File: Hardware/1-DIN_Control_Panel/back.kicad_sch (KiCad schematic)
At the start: 44 parts, among them J1 Mode LEDs, J1 Selector Knob Connector, J2 Rotary Switch 1x7, J3 2x05 Molex Micro-Fit 3.0 43045, J4 UART Expansion, J5 SW - Aux Jump-Start, J6 SW - Battery Bypass, J7 SW - Master Power, J8 Pot/SW - Brightness, K1 FINDER-40.52, U12 LM324DR, U13 12V->5V Variable Boost Buck C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, U5 LTV-847S, U6 LTV-847S

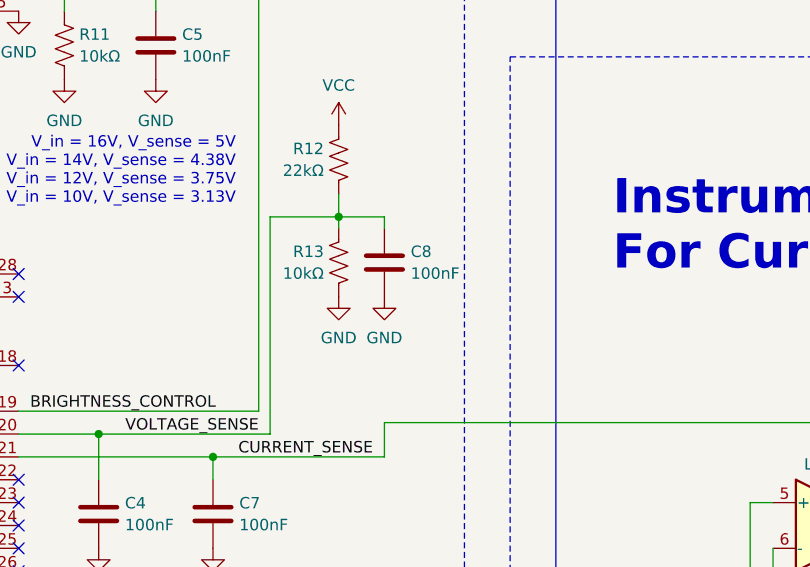
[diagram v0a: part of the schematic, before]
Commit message: Finished routing of rear board
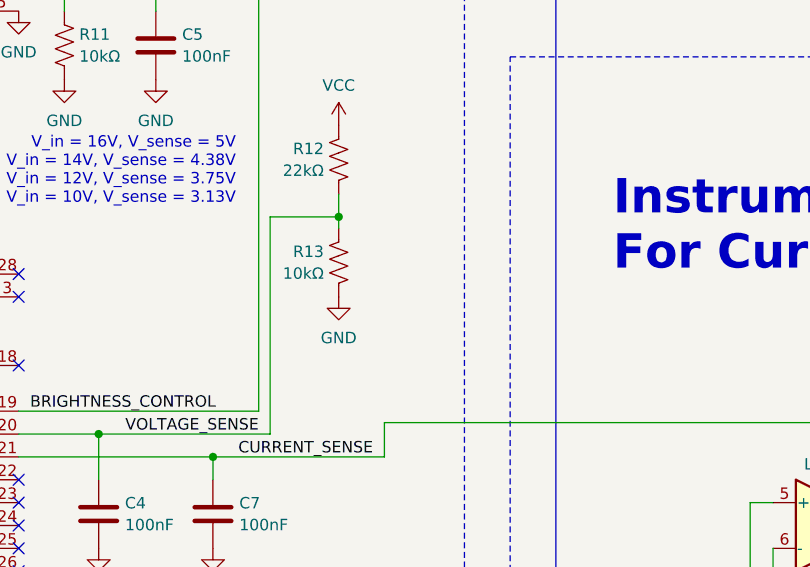
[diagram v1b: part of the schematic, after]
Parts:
- removed C8: 100nF, Capacitor_SMD:C_0603_1608Metric_Pad1.08x0.95mm_HandSolder, symbol Device:C
- C11, C14: footprint Capacitor_SMD:C_0603_1608Metric_Pad1.08x0.95mm_HandSolder -> Capacitor_SMD:C_1206_3216Metric_Pad1.33x1.80mm_HandSolder
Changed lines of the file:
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@@
     (stroke (width 0) (type default))
   )
-  (wire (pts (xy 256.54 116.84) (xy 251.46 116.84))
-    (stroke (width 0) (type default))
-  )
   (wire (pts (xy 360.68 40.64) (xy 360.68 39.37))
     (stroke (width 0) (type default))
   )
-  (wire (pts (xy 256.54 118.11) (xy 256.54 116.84))
-    (stroke (width 0) (type default))
-  )
   (wire (pts (xy 281.94 170.18) (xy 297.18 170.18))
     (stroke (width 0) (type default))
@@
       (effects (font (size 1.27 1.27)) (justify right))
     )
-    (property "Footprint" "Capacitor_SMD:C_0603_1608Metric_Pad1.08x0.95mm_HandSolder" (at 368.6048 46.99 0)
+    (property "Footprint" "Capacitor_SMD:C_1206_3216Metric_Pad1.33x1.80mm_HandSolder" (at 368.6048 46.99 0)
       (effects (font (size 1.27 1.27)) hide)
     )
@@
     )
   )
-  (symbol (lib_id "power:GND") (at 256.54 125.73 0) (unit 1)
-    (in_bom yes) (on_board yes) (dnp no) (fields_autoplaced)
-    (property "Reference" "#PWR021" (at 256.54 132.08 0)
-      (effects (font (size 1.27 1.27)) hide)
-    )
-    (property "Value" "GND" (at 256.54 130.2925 0)
-      (effects (font (size 1.27 1.27)))
-    )
-    (property "Footprint" "" (at 256.54 125.73 0)
-      (effects (font (size 1.27 1.27)) hide)
-    )
-    (property "Datasheet" "" (at 256.54 125.73 0)
-      (effects (font (size 1.27 1.27)) hide)
-    )
-    (pin "1")
-    (instances
-      (project "1-DIN_Control_Panel"
-        (path "/9d6c5460-8470-44bf-9076-df961456f999"
-          (reference "#PWR021") (unit 1)
-        )
-        (path "/9d6c5460-8470-44bf-9076-df961456f999/79705e83-d37e-491a-a216-1b060693c97a"
-          (reference "#PWR021") (unit 1)
-        )
-      )
-    )
-  )
   (symbol (lib_id "power:GND") (at 220.98 101.6 0) (mirror y) (unit 1)
     (in_bom yes) (on_board yes) (dnp no) (fields_autoplaced)
@@
     )
   )
-  (symbol (lib_id "Device:C") (at 256.54 121.92 0) (unit 1)
-    (in_bom yes) (on_board yes) (dnp no) (fields_autoplaced)
-    (property "Reference" "C8" (at 259.461 120.7079 0)
-      (effects (font (size 1.27 1.27)) (justify left))
-    )
-    (property "Value" "100nF" (at 259.461 123.1321 0)
-      (effects (font (size 1.27 1.27)) (justify left))
-    )
-    (property "Footprint" "Capacitor_SMD:C_0603_1608Metric_Pad1.08x0.95mm_HandSolder" (at 257.5052 125.73 0)
-      (effects (font (size 1.27 1.27)) hide)
-    )
-    (property "Datasheet" "~" (at 256.54 121.92 0)
-      (effects (font (size 1.27 1.27)) hide)
-    )
-    (pin "1")
-    (pin "2")
-    (instances
-      (project "1-DIN_Control_Panel"
-        (path "/9d6c5460-8470-44bf-9076-df961456f999"
-          (reference "C8") (unit 1)
-        )
-        (path "/9d6c5460-8470-44bf-9076-df961456f999/79705e83-d37e-491a-a216-1b060693c97a"
-          (reference "C8") (unit 1)
-        )
-      )
-    )
-  )
   (symbol (lib_id "power:GND") (at 251.46 125.73 0) (unit 1)
     (in_bom yes) (on_board yes) (dnp no) (fields_autoplaced)
@@
       (effects (font (size 1.27 1.27)) (justify right))
     )
-    (property "Footprint" "Capacitor_SMD:C_0603_1608Metric_Pad1.08x0.95mm_HandSolder" (at 328.6252 45.72 0)
+    (property "Footprint" "Capacitor_SMD:C_1206_3216Metric_Pad1.33x1.80mm_HandSolder" (at 328.6252 45.72 0)
       (effects (font (size 1.27 1.27)) hide)
     )

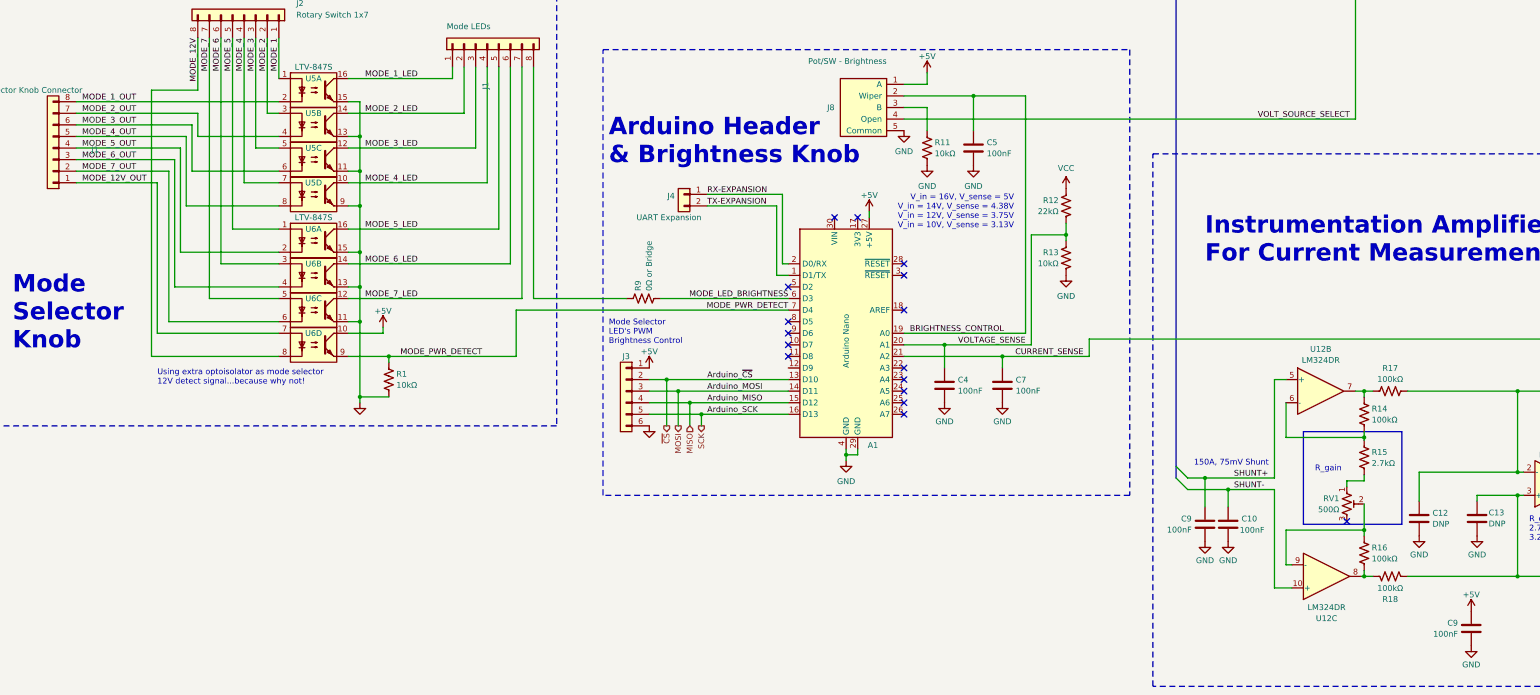
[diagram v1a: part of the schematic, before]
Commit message: Finished routing front panel
Realized that I don't know how optocouplers work, so I need to replace them with transistors or something now
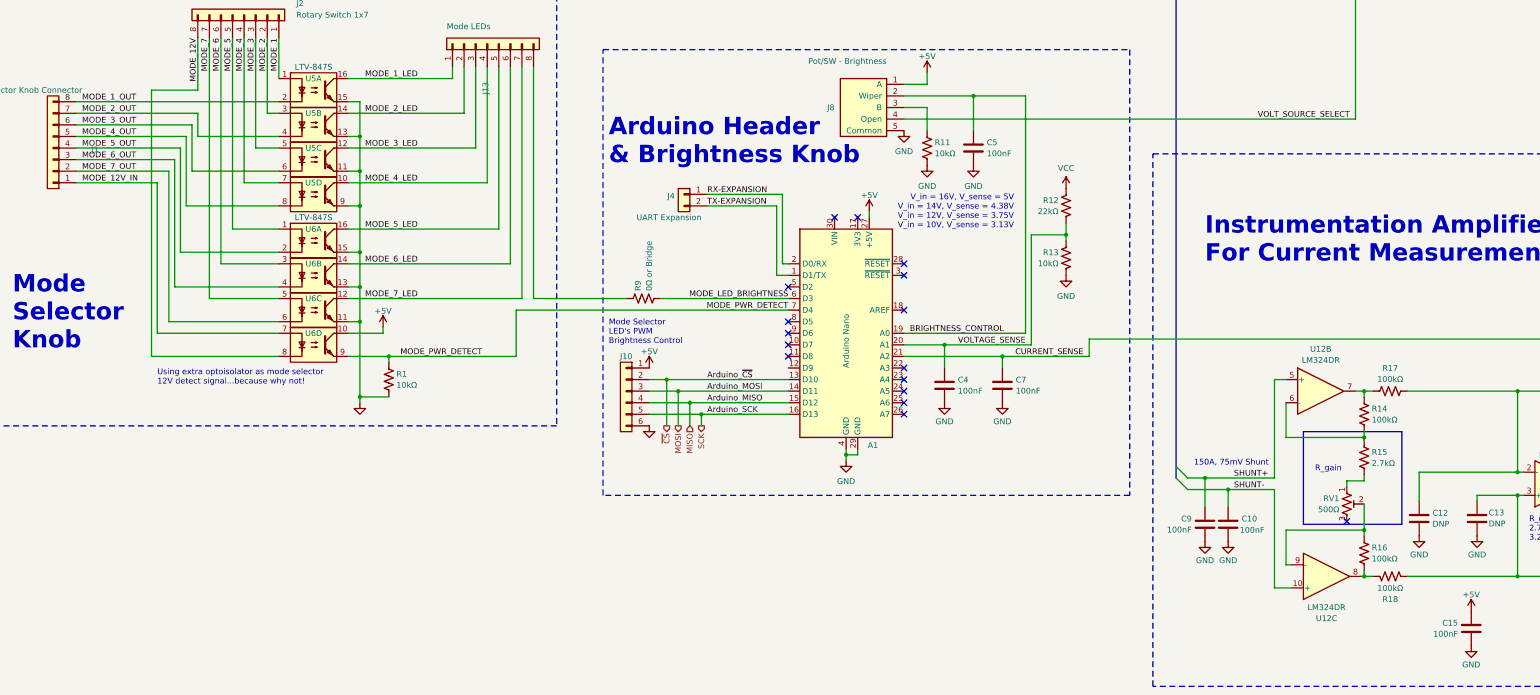
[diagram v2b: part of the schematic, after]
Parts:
- C11, C14: footprint Capacitor_SMD:C_1206_3216Metric_Pad1.33x1.80mm_HandSolder -> Capacitor_Tantalum_SMD:CP_EIA-3528-21_Kemet-B_Pad1.50x2.35mm_HandSolder
- F1: footprint Fuse:Fuse_Bourns_MF-RG300 -> Fuse:Fuse_1812_4532Metric_Pad1.30x3.40mm_HandSolder
- renumbered C9 to C15, J3 to J10, J1 to J13
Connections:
- net MODE_12V_OUT renamed MODE_12V_IN

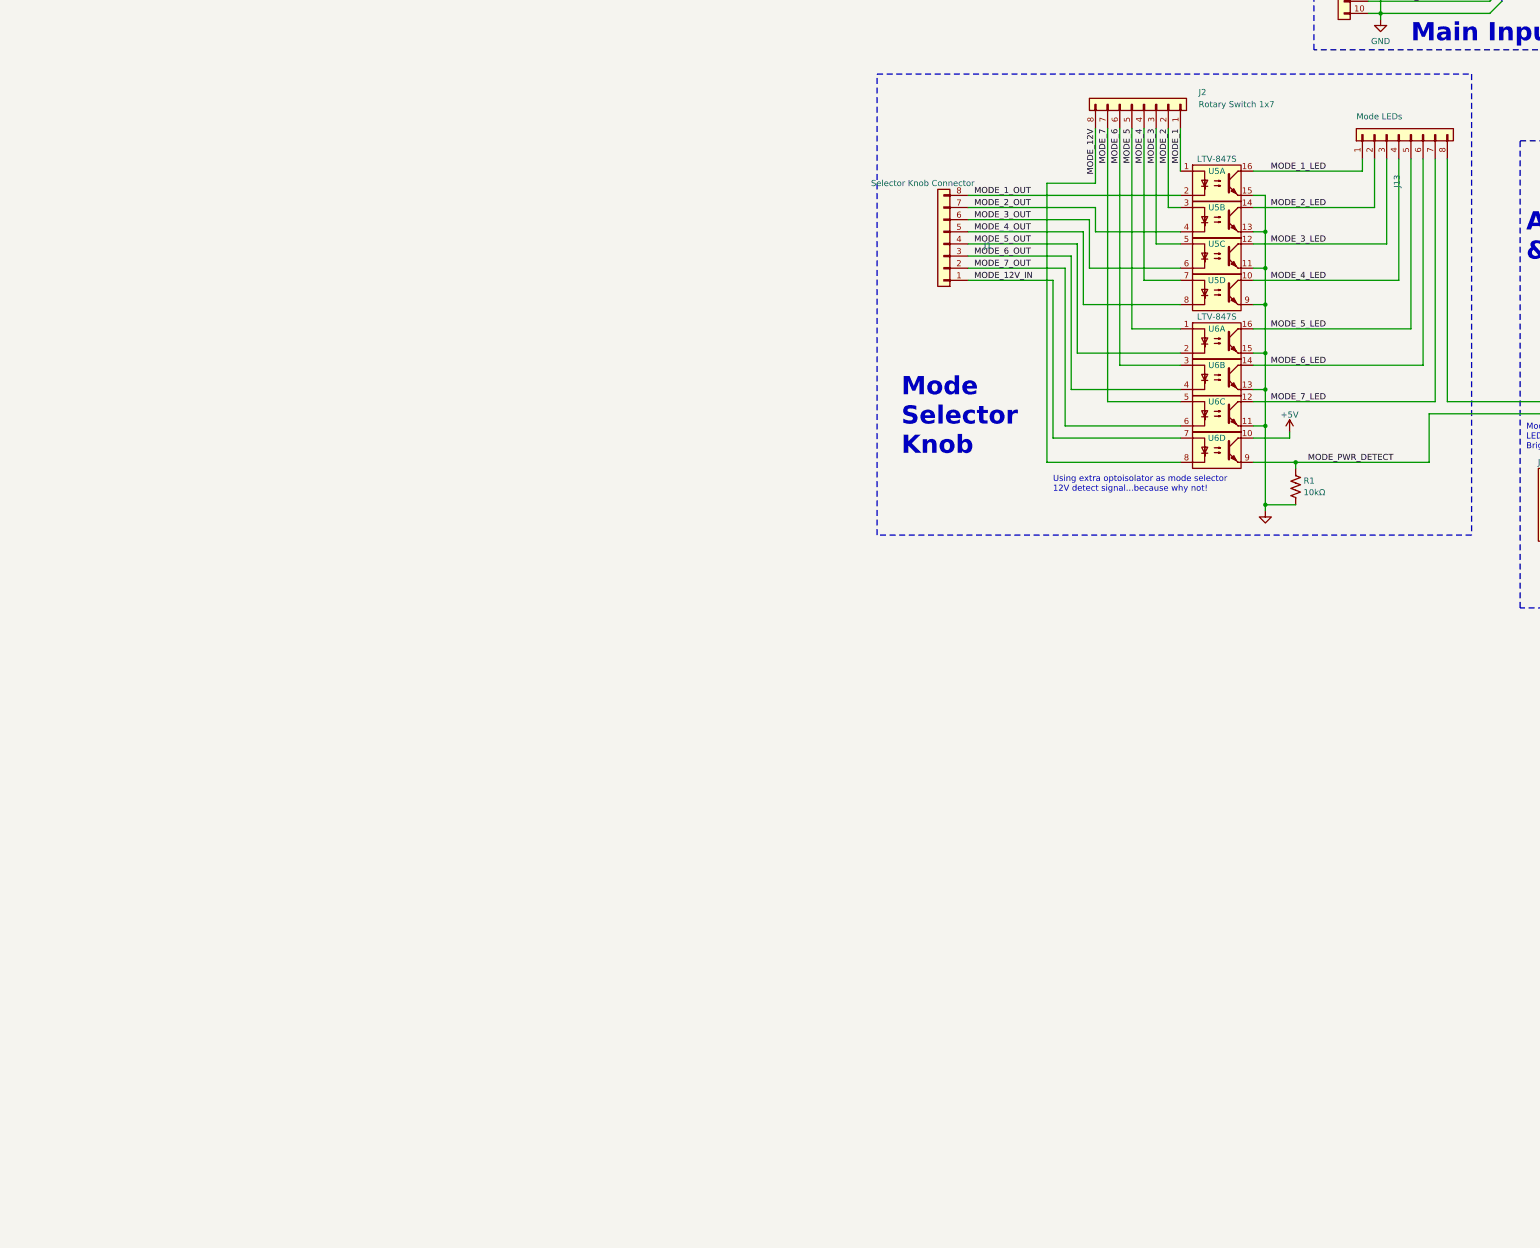
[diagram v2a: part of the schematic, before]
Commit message: Beginning to transition to BJTs
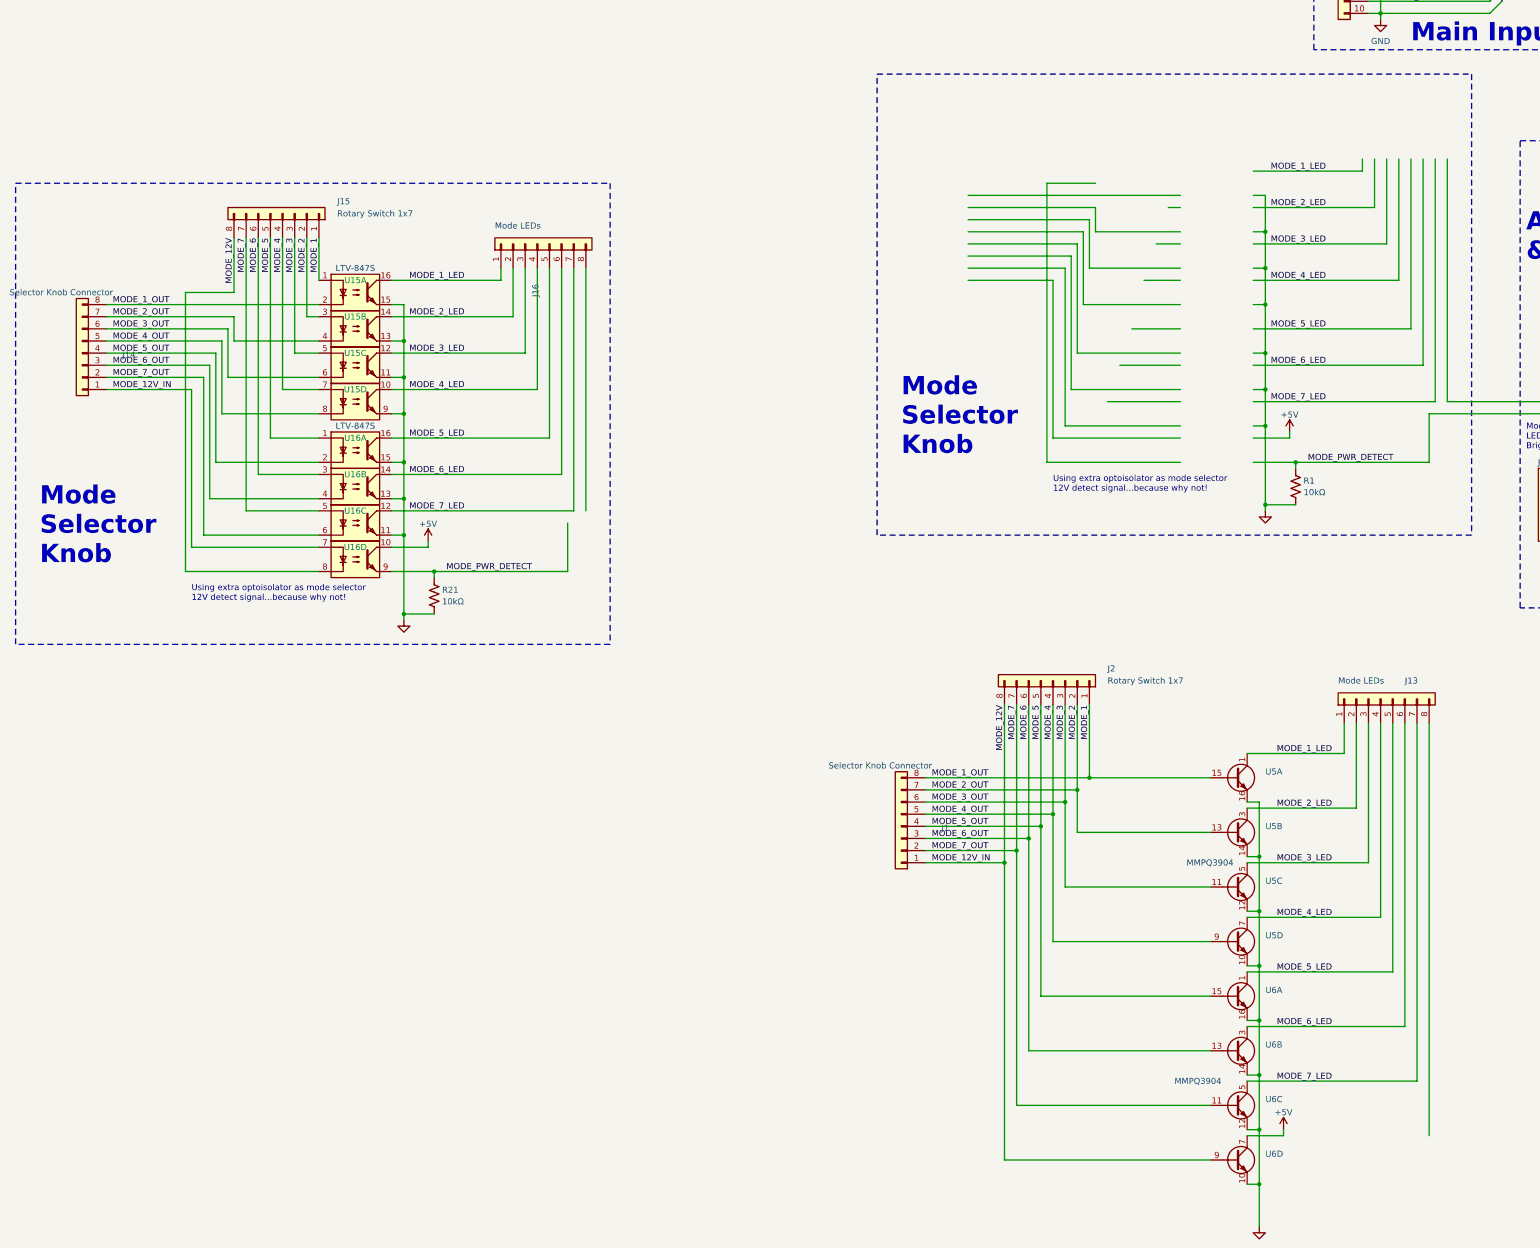
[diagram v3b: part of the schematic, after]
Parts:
- removed U5, U6: LTV-847S, Package_DIP:SMDIP-16_W9.53mm, symbol Isolator:LTV-847S
- added J14: Selector Knob Connector, Connector_Molex:Molex_Micro-Fit_3.0_43045-0812_2x04_P3.00mm_Vertical, symbol Connector_Generic:Conn_01x08
- added J15: Rotary Switch 1x7, Connector_Molex:Molex_Micro-Fit_3.0_43045-0812_2x04_P3.00mm_Vertical, symbol Connector_Generic:Conn_01x08
- added J16: Mode LEDs, Connector_Molex:Molex_Micro-Fit_3.0_43045-0812_2x04_P3.00mm_Vertical, symbol Connector_Generic:Conn_01x08
- added R21: 10kΩ, Resistor_SMD:R_0603_1608Metric_Pad0.98x0.95mm_HandSolder, symbol Device:R_US
- added U15, U16: LTV-847S, Package_DIP:SMDIP-16_W9.53mm, symbol Isolator:LTV-847S
- added U5, U6: MMPQ3904, Package_SO:SOIC-16_4.55x10.3mm_P1.27mm, symbol Panel_Parts:MMPQ3904
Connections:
- net MODE_12V_IN is gone; now on net MODE_12V: J1.1 (Pin_1)
- net MODE_1_OUT is gone; now on net MODE_1: J1.8 (Pin_8)
- net MODE_2_OUT is gone; now on net MODE_2: J1.7 (Pin_7)
- net MODE_3_OUT is gone; now on net MODE_3: J1.6 (Pin_6)
- net MODE_4_OUT is gone; now on net MODE_4: J1.5 (Pin_5)
- net MODE_5_OUT is gone; now on net MODE_5: J1.4 (Pin_4)
- net MODE_6_OUT is gone; now on net MODE_6: J1.3 (Pin_3)
- net MODE_7_OUT is gone; now on net MODE_7: J1.2 (Pin_2)
- net +5V: now also U16.10, U6.7 (C4), U6.8 (C4)
- net GND: now also R21.1, U15.11, U15.13, U15.15, U15.9, U16.11, U16.13, U16.15, U5.10 (E4), U5.12 (E3), U5.14 (E2), U5.16 (E1), U6.10 (E4), U6.12 (E3), U6.14 (E2), U6.16 (E1)
- net MODE_1: now also J14.8 (Pin_8), J15.1 (Pin_1), U15.1, U15.2, U5.15 (B1)
- net MODE_12V: now also J14.1 (Pin_1), J15.8 (Pin_8), U16.7, U16.8, U6.9 (B4)
- net MODE_1_LED: now also J16.1 (Pin_1), U15.16, U5.1 (C1), U5.2 (C1)
- net MODE_2: now also J14.7 (Pin_7), J15.2 (Pin_2), U15.3, U15.4, U5.13 (B2)
- net MODE_2_LED: now also J16.2 (Pin_2), U15.14, U5.3 (C2), U5.4 (C2)
- net MODE_3: now also J14.6 (Pin_6), J15.3 (Pin_3), U15.5, U15.6, U5.11 (B3)
- net MODE_3_LED: now also J16.3 (Pin_3), U15.12, U5.5 (C4), U5.6 (C3)
- net MODE_4: now also J14.5 (Pin_5), J15.4 (Pin_4), U15.7, U15.8, U5.9 (B4)
- net MODE_4_LED: now also J16.4 (Pin_4), U15.10, U5.7 (C4), U5.8 (C4)
- net MODE_5: now also J14.4 (Pin_4), J15.5 (Pin_5), U16.1, U16.2, U6.15 (B1)
- net MODE_5_LED: now also J16.5 (Pin_5), U16.16, U6.1 (C1), U6.2 (C1)
- net MODE_6: now also J14.3 (Pin_3), J15.6 (Pin_6), U16.3, U16.4, U6.13 (B2)
- net MODE_6_LED: now also J16.6 (Pin_6), U16.14, U6.3 (C2), U6.4 (C2)
- net MODE_7: now also J14.2 (Pin_2), J15.7 (Pin_7), U16.5, U16.6, U6.11 (B3)
- net MODE_7_LED: now also J16.7 (Pin_7), U16.12, U6.5 (C4), U6.6 (C3)
- net MODE_PWR_DETECT: now also R21.2, U16.9
- net at J13.8 (Pin_8): no longer R9.2
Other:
- moved on the sheet: J1, J13, J2
